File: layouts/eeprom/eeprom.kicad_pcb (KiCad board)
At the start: 2 copper layers, 2 parts

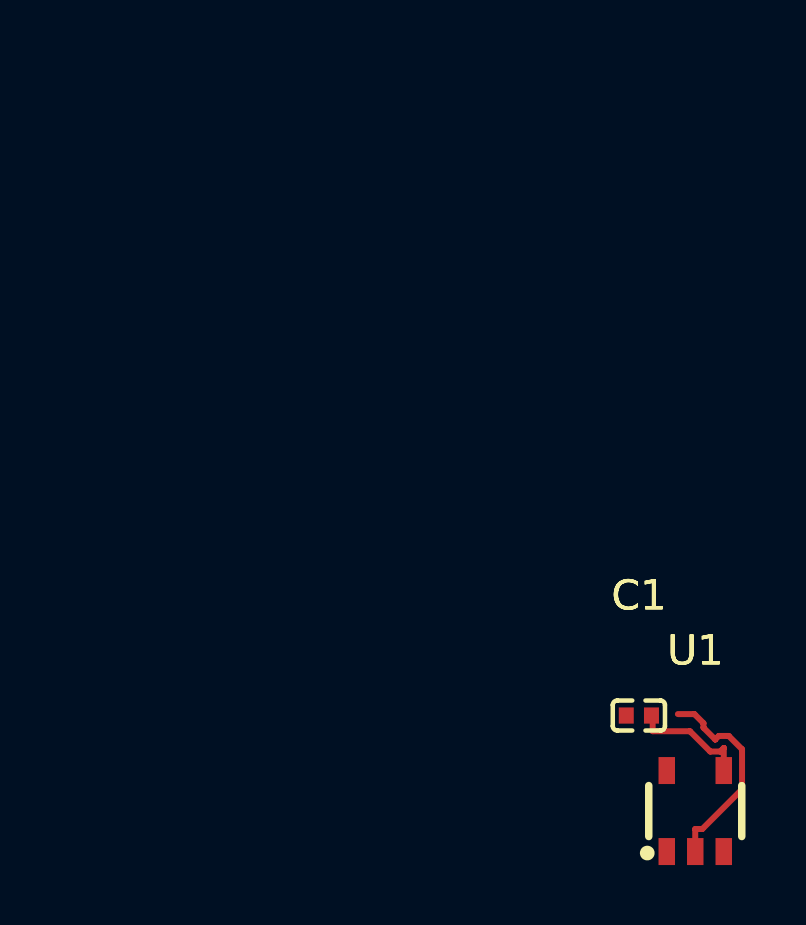
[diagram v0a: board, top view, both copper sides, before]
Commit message: Enhance smart placer with simulated annealing and pre-routing validation
Smart Placer improvements:
- Add simulated annealing refinement (now default) for better wire length optimization
- Add force-directed refinement with improvement safeguard
- Add silkscreen text repositioning to avoid component overlaps
- Significant wire length reductions (e.g., power_filter: 113mm -> 46mm)

Autorouter improvements:
- Add PreRoutingValidator class for pre-flight checks
- Validate unconnected pads, overlapping footprints, unplaced components
- Use pad-based bounds for accurate overlap detection
- Block routing on validation errors with actionable messages

Research:
- Add comprehensive autorouting/autoplacement findings document
- Cover Freerouting Python client, OrthoRoute, DeepPCB, KiCad 9 IPC API
- Document force-directed and simulated annealing algorithms

Cleanup:
- Update .gitignore for DSN/SES files, build artifacts, tools
- Remove stale timestamped build files
- Add parts footprints and symbols

All 10 modules placed and routed successfully.

Co-Authored-By: Claude Opus 4.5 <noreply@anthropic.com>
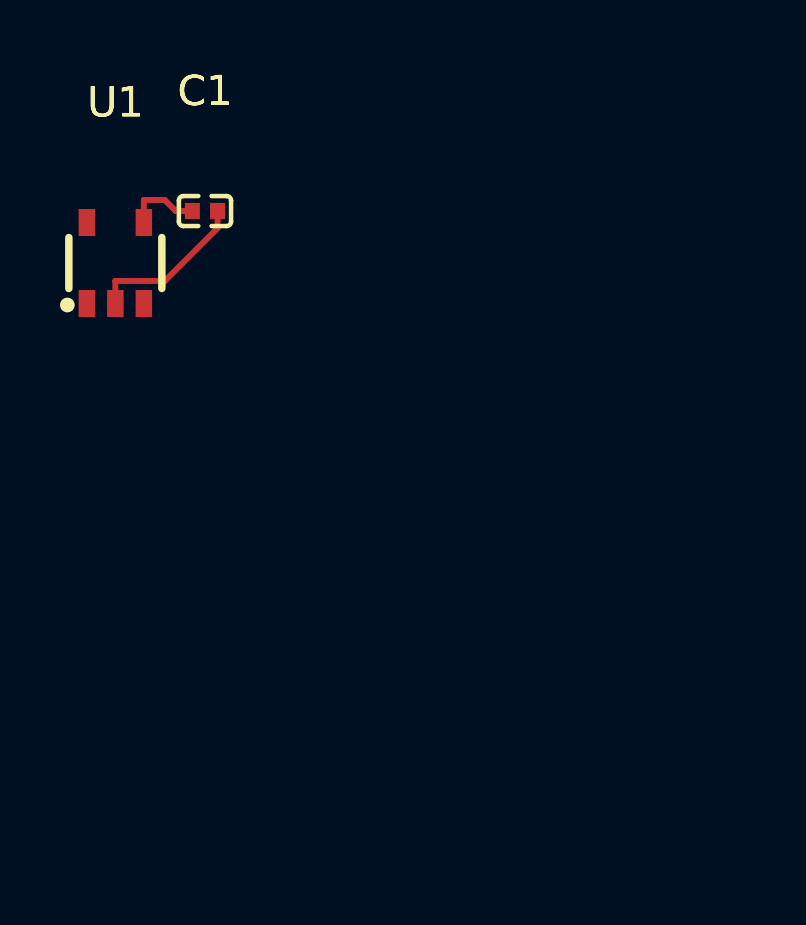
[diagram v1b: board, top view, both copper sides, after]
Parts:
- moved U1 26.6 mm to (80.7, 81.7)
- moved C1 22.2 mm to (83.7, 80.0)
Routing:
- net GND: track 7.01 -> 5.46 mm
- net VCC: track 4.02 -> 2.52 mm
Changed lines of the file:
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@@
 	(footprint "Samsung_Electro_Mechanics_CL05B104KO5NNNC:C0402"
 		(layer "F.Cu")
-		(at 98.120614 96.815959)
+		(at 83.6574 80)
 		(property "Reference" "C1"
 			(at 0 -4 0)
@@
 	(footprint "FMD_FT24C02A_KLR_T:SOT-23-5_L2.9-W1.5-P0.95-LS2.8-BL"
 		(layer "F.Cu")
-		(at 100 100)
+		(at 80.6698 81.732)
 		(property "Reference" "U1"
 			(at 0 -5.35 0)
@@
 	)
 	(segment
-		(start 98.58 97.3396)
-		(end 99.8233 97.3396)
+		(start 81.6198 80.382)
+		(end 81.6198 79.6303)
 		(width 0.2)
 		(layer "F.Cu")
@@
 	)
 	(segment
-		(start 100.9499 97.8983)
-		(end 100.95 97.8983)
+		(start 82.316 79.6303)
+		(end 82.6857 80)
 		(width 0.2)
 		(layer "F.Cu")
@@
 	)
 	(segment
-		(start 99.8233 97.3396)
-		(end 100.4997 98.016)
+		(start 81.6198 79.6303)
+		(end 82.316 79.6303)
 		(width 0.2)
 		(layer "F.Cu")
@@
 	)
 	(segment
-		(start 98.58 96.7679)
-		(end 98.58 97.3396)
+		(start 83.2374 80)
+		(end 82.6857 80)
 		(width 0.2)
 		(layer "F.Cu")
@@
 	)
 	(segment
-		(start 100.95 98.65)
-		(end 100.95 97.8983)
-		(width 0.2)
-		(layer "F.Cu")
-		(net 2)
-	)
-	(segment
-		(start 100.8322 98.016)
-		(end 100.9499 97.8983)
-		(width 0.2)
-		(layer "F.Cu")
-		(net 2)
-	)
-	(segment
-		(start 100.4997 98.016)
-		(end 100.8322 98.016)
-		(width 0.2)
-		(layer "F.Cu")
-		(net 2)
-	)
-	(segment
-		(start 100.6659 97.6142)
-		(end 100.2739 97.2222)
+		(start 80.6698 82.3303)
+		(end 82.3188 82.3303)
 		(width 0.2)
 		(layer "F.Cu")
@@
 	)
 	(segment
-		(start 101.1164 97.4966)
-		(end 100.7836 97.4966)
+		(start 82.3188 82.3303)
+		(end 84.0774 80.5717)
 		(width 0.2)
 		(layer "F.Cu")
@@
 	)
 	(segment
-		(start 100.666 97.6142)
-		(end 100.6659 97.6142)
+		(start 80.6698 83.082)
+		(end 80.6698 82.3303)
 		(width 0.2)
 		(layer "F.Cu")
@@
 	)
 	(segment
-		(start 100.2739 97.2222)
-		(end 100.2739 97.0701)
-		(width 0.2)
-		(layer "F.Cu")
-		(net 4)
-	)
-	(segment
-		(start 101.5597 99.2738)
-		(end 101.5597 97.9399)
-		(width 0.2)
-		(layer "F.Cu")
-		(net 4)
-	)
-	(segment
-		(start 100.2739 97.0701)
-		(end 99.9717 96.7679)
-		(width 0.2)
-		(layer "F.Cu")
-		(net 4)
-	)
-	(segment
-		(start 100 101.35)
-		(end 100 100.5983)
-		(width 0.2)
-		(layer "F.Cu")
-		(net 4)
-	)
-	(segment
-		(start 100.2352 100.5983)
-		(end 101.5597 99.2738)
-		(width 0.2)
-		(layer "F.Cu")
-		(net 4)
-	)
-	(segment
-		(start 101.5597 97.9399)
-		(end 101.1164 97.4966)
-		(width 0.2)
-		(layer "F.Cu")
-		(net 4)
-	)
-	(segment
-		(start 100 100.5983)
-		(end 100.2352 100.5983)
-		(width 0.2)
-		(layer "F.Cu")
-		(net 4)
-	)
-	(segment
-		(start 99.42 96.7679)
-		(end 99.9717 96.7679)
-		(width 0.2)
-		(layer "F.Cu")
-		(net 4)
-	)
-	(segment
-		(start 100.7836 97.4966)
-		(end 100.666 97.6142)
-		(width 0.2)
-		(layer "F.Cu")
+		(start 84.0774 80)
+		(end 84.0774 80.5717)
+		(width 0.2)
+		(layer "F.Cu")
